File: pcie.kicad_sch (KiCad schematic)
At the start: 28 parts, among them J10 1-2199119-6, U1 MIMX8MM6DVTLZAA, U33 SI52112-B5-GM2, U34 74LVC2G07, Y4 25MHz

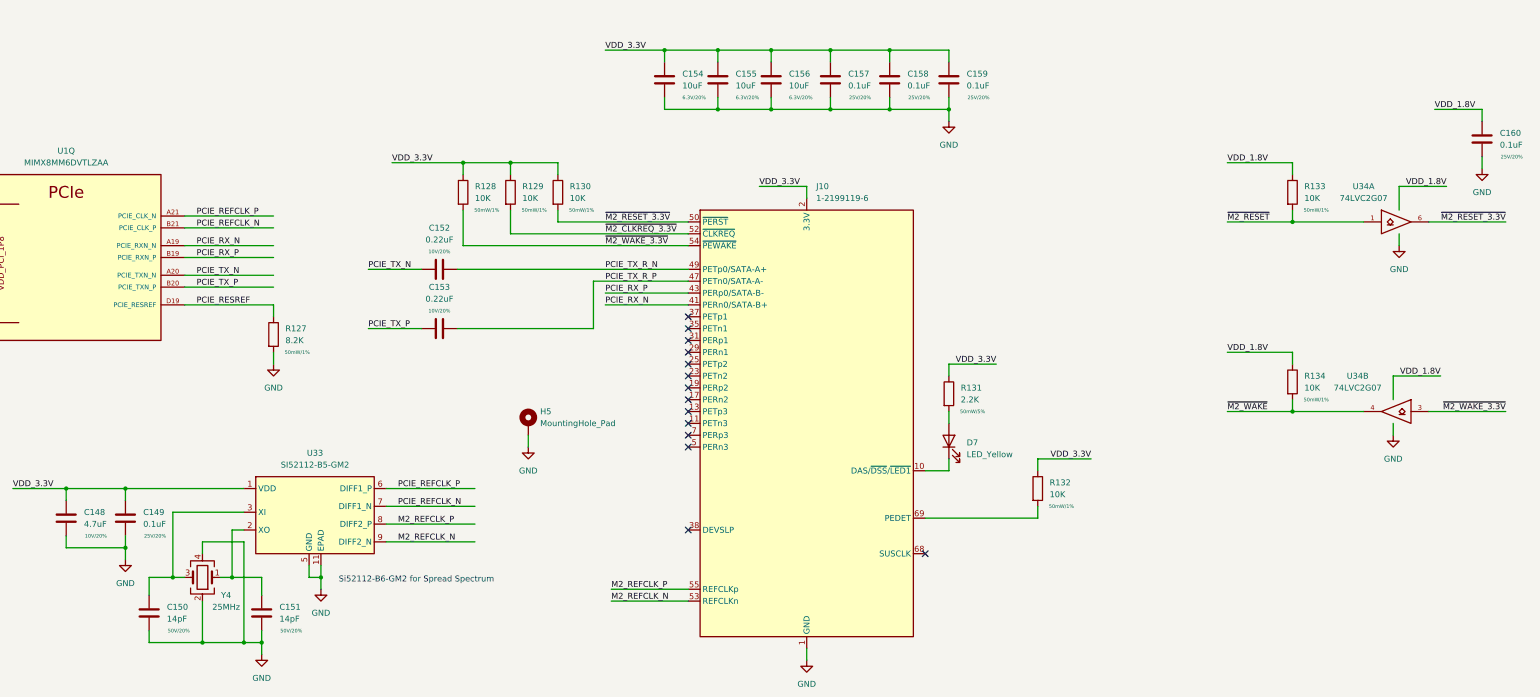
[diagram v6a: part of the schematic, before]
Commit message: ddr length matching work, misc cleanup
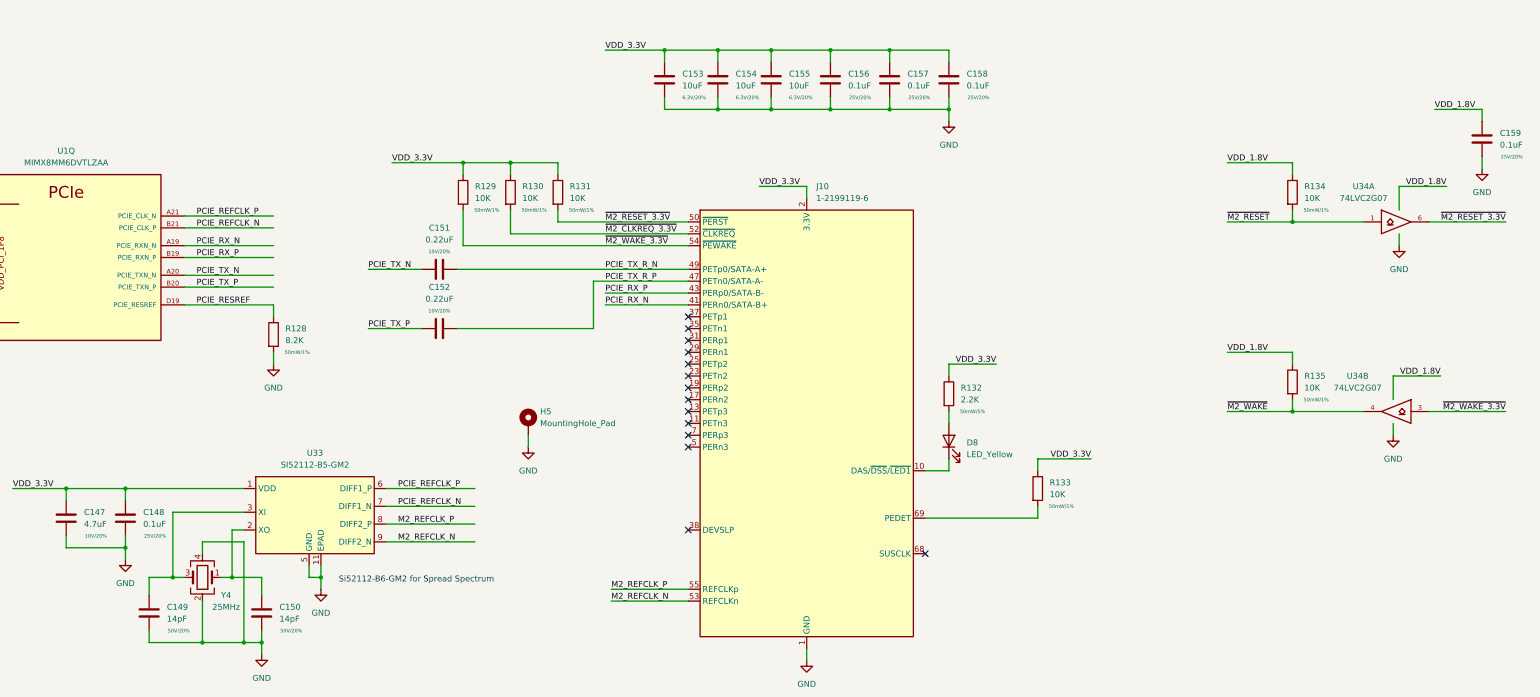
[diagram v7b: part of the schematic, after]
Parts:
- renumbered C148 to C147, C149 to C148, C150 to C149, C151 to C150, C152 to C151, C153 to C152, C154 to C153, C155 to C154, C156 to C155, C157 to C156, C158 to C157, C159 to C158, C160 to C159, D7 to D8, R127 to R128, R128 to R129, R129 to R130, R130 to R131, R131 to R132, R132 to R133, R133 to R134, R134 to R135
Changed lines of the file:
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@@
   (symbol (lib_id "power:GND") (at 236.22 154.94 0) (unit 1)
     (in_bom yes) (on_board yes) (fields_autoplaced)
-    (property "Reference" "#PWR0148" (id 0) (at 236.22 161.29 0)
+    (property "Reference" "#PWR0151" (id 0) (at 236.22 161.29 0)
       (effects (font (size 1.27 1.27)) hide)
     )
@@
   (symbol (lib_id "Device:C") (at 381 43.18 0) (unit 1)
     (in_bom yes) (on_board yes)
-    (property "Reference" "C160" (id 0) (at 384.81 41.9099 0)
+    (property "Reference" "C159" (id 0) (at 384.81 41.9099 0)
       (effects (font (size 1.27 1.27)) (justify left))
     )
@@
   (symbol (lib_id "Device:C") (at 254 30.48 0) (unit 1)
     (in_bom yes) (on_board yes)
-    (property "Reference" "C158" (id 0) (at 257.81 29.2099 0)
+    (property "Reference" "C157" (id 0) (at 257.81 29.2099 0)
       (effects (font (size 1.27 1.27)) (justify left))
     )
@@
   (symbol (lib_id "Device:R") (at 266.7 97.79 0) (unit 1)
     (in_bom yes) (on_board yes)
-    (property "Reference" "R131" (id 0) (at 269.24 96.5199 0)
+    (property "Reference" "R132" (id 0) (at 269.24 96.5199 0)
       (effects (font (size 1.27 1.27)) (justify left))
     )
@@
   (symbol (lib_id "power:GND") (at 119.38 153.67 0) (unit 1)
     (in_bom yes) (on_board yes) (fields_autoplaced)
-    (property "Reference" "#PWR0144" (id 0) (at 119.38 160.02 0)
+    (property "Reference" "#PWR0147" (id 0) (at 119.38 160.02 0)
       (effects (font (size 1.27 1.27)) hide)
     )
@@
   (symbol (lib_id "power:GND") (at 266.7 39.37 0) (unit 1)
     (in_bom yes) (on_board yes) (fields_autoplaced)
-    (property "Reference" "#PWR0149" (id 0) (at 266.7 45.72 0)
+    (property "Reference" "#PWR0152" (id 0) (at 266.7 45.72 0)
       (effects (font (size 1.27 1.27)) hide)
     )
@@
   (symbol (lib_id "Device:C") (at 266.7 30.48 0) (unit 1)
     (in_bom yes) (on_board yes)
-    (property "Reference" "C159" (id 0) (at 270.51 29.2099 0)
+    (property "Reference" "C158" (id 0) (at 270.51 29.2099 0)
       (effects (font (size 1.27 1.27)) (justify left))
     )
@@
   (symbol (lib_id "Device:C") (at 228.6 30.48 0) (unit 1)
     (in_bom yes) (on_board yes)
-    (property "Reference" "C156" (id 0) (at 232.41 29.2099 0)
+    (property "Reference" "C155" (id 0) (at 232.41 29.2099 0)
       (effects (font (size 1.27 1.27)) (justify left))
     )
@@
   (symbol (lib_id "power:GND") (at 121.92 91.44 0) (unit 1)
     (in_bom yes) (on_board yes) (fields_autoplaced)
-    (property "Reference" "#PWR0145" (id 0) (at 121.92 97.79 0)
+    (property "Reference" "#PWR0148" (id 0) (at 121.92 97.79 0)
       (effects (font (size 1.27 1.27)) hide)
     )
@@
   (symbol (lib_id "Device:R") (at 121.92 85.09 0) (unit 1)
     (in_bom yes) (on_board yes)
-    (property "Reference" "R127" (id 0) (at 124.46 83.8199 0)
+    (property "Reference" "R128" (id 0) (at 124.46 83.8199 0)
       (effects (font (size 1.27 1.27)) (justify left))
     )
@@
   (symbol (lib_id "Device:C") (at 241.3 30.48 0) (unit 1)
     (in_bom yes) (on_board yes)
-    (property "Reference" "C157" (id 0) (at 245.11 29.2099 0)
+    (property "Reference" "C156" (id 0) (at 245.11 29.2099 0)
       (effects (font (size 1.27 1.27)) (justify left))
     )
@@
   (symbol (lib_id "Device:C") (at 90.17 124.46 0) (unit 1)
     (in_bom yes) (on_board yes)
-    (property "Reference" "C149" (id 0) (at 93.98 123.1899 0)
+    (property "Reference" "C148" (id 0) (at 93.98 123.1899 0)
       (effects (font (size 1.27 1.27)) (justify left))
     )
@@
   (symbol (lib_id "Device:R") (at 340.36 54.61 0) (unit 1)
     (in_bom yes) (on_board yes)
-    (property "Reference" "R133" (id 0) (at 342.9 53.3399 0)
+    (property "Reference" "R134" (id 0) (at 342.9 53.3399 0)
       (effects (font (size 1.27 1.27)) (justify left))
     )
@@
   (symbol (lib_id "Device:C") (at 95.25 144.78 0) (unit 1)
     (in_bom yes) (on_board yes)
-    (property "Reference" "C150" (id 0) (at 99.06 143.5099 0)
+    (property "Reference" "C149" (id 0) (at 99.06 143.5099 0)
       (effects (font (size 1.27 1.27)) (justify left))
     )
@@
   (symbol (lib_id "Device:R") (at 172.72 54.61 0) (unit 1)
     (in_bom yes) (on_board yes)
-    (property "Reference" "R129" (id 0) (at 175.26 53.3399 0)
+    (property "Reference" "R130" (id 0) (at 175.26 53.3399 0)
       (effects (font (size 1.27 1.27)) (justify left))
     )
@@
   (symbol (lib_id "Device:R") (at 285.75 118.11 0) (unit 1)
     (in_bom yes) (on_board yes)
-    (property "Reference" "R132" (id 0) (at 288.29 116.8399 0)
+    (property "Reference" "R133" (id 0) (at 288.29 116.8399 0)
       (effects (font (size 1.27 1.27)) (justify left))
     )
@@
   (symbol (lib_id "Device:C") (at 157.48 83.82 90) (unit 1)
     (in_bom yes) (on_board yes)
-    (property "Reference" "C153" (id 0) (at 157.48 74.93 90))
+    (property "Reference" "C152" (id 0) (at 157.48 74.93 90))
     (property "Value" "0.22uF" (id 1) (at 157.48 77.47 90))
     (property "Footprint" "qsbc:C_0201_0603Metric" (id 2) (at 161.29 82.8548 0)
@@
   (symbol (lib_id "Device:R") (at 182.88 54.61 0) (unit 1)
     (in_bom yes) (on_board yes)
-    (property "Reference" "R130" (id 0) (at 185.42 53.3399 0)
+    (property "Reference" "R131" (id 0) (at 185.42 53.3399 0)
       (effects (font (size 1.27 1.27)) (justify left))
     )
@@
   (symbol (lib_id "power:GND") (at 90.17 133.35 0) (unit 1)
     (in_bom yes) (on_board yes) (fields_autoplaced)
-    (property "Reference" "#PWR0143" (id 0) (at 90.17 139.7 0)
+    (property "Reference" "#PWR0146" (id 0) (at 90.17 139.7 0)
       (effects (font (size 1.27 1.27)) hide)
     )
@@
   (symbol (lib_id "power:GND") (at 361.95 106.68 0) (unit 1)
     (in_bom yes) (on_board yes) (fields_autoplaced)
-    (property "Reference" "#PWR0150" (id 0) (at 361.95 113.03 0)
+    (property "Reference" "#PWR0153" (id 0) (at 361.95 113.03 0)
       (effects (font (size 1.27 1.27)) hide)
     )
@@
   (symbol (lib_id "power:GND") (at 363.22 66.04 0) (unit 1)
     (in_bom yes) (on_board yes) (fields_autoplaced)
-    (property "Reference" "#PWR0151" (id 0) (at 363.22 72.39 0)
+    (property "Reference" "#PWR0154" (id 0) (at 363.22 72.39 0)
       (effects (font (size 1.27 1.27)) hide)
     )
@@
   (symbol (lib_id "Device:C") (at 119.38 144.78 0) (unit 1)
     (in_bom yes) (on_board yes)
-    (property "Reference" "C151" (id 0) (at 123.19 143.5099 0)
+    (property "Reference" "C150" (id 0) (at 123.19 143.5099 0)
       (effects (font (size 1.27 1.27)) (justify left))
     )
@@
   (symbol (lib_id "Device:C") (at 77.47 124.46 0) (unit 1)
     (in_bom yes) (on_board yes)
-    (property "Reference" "C148" (id 0) (at 81.28 123.1899 0)
+    (property "Reference" "C147" (id 0) (at 81.28 123.1899 0)
       (effects (font (size 1.27 1.27)) (justify left))
     )
@@
   (symbol (lib_id "power:GND") (at 381 49.53 0) (unit 1)
     (in_bom yes) (on_board yes) (fields_autoplaced)
-    (property "Reference" "#PWR0152" (id 0) (at 381 55.88 0)
+    (property "Reference" "#PWR0155" (id 0) (at 381 55.88 0)
       (effects (font (size 1.27 1.27)) hide)
     )
@@
   (symbol (lib_id "Device:R") (at 162.56 54.61 0) (unit 1)
     (in_bom yes) (on_board yes)
-    (property "Reference" "R128" (id 0) (at 165.1 53.3399 0)
+    (property "Reference" "R129" (id 0) (at 165.1 53.3399 0)
       (effects (font (size 1.27 1.27)) (justify left))
     )
@@
   (symbol (lib_id "Device:LED") (at 266.7 107.95 90) (unit 1)
     (in_bom yes) (on_board yes) (fields_autoplaced)
-    (property "Reference" "D7" (id 0) (at 270.51 108.2674 90)
+    (property "Reference" "D8" (id 0) (at 270.51 108.2674 90)
       (effects (font (size 1.27 1.27)) (justify right))
     )
@@
   (symbol (lib_id "power:GND") (at 132.08 139.7 0) (unit 1)
     (in_bom yes) (on_board yes) (fields_autoplaced)
-    (property "Reference" "#PWR0146" (id 0) (at 132.08 146.05 0)
+    (property "Reference" "#PWR0149" (id 0) (at 132.08 146.05 0)
       (effects (font (size 1.27 1.27)) hide)
     )
@@
   (symbol (lib_id "Device:C") (at 217.17 30.48 0) (unit 1)
     (in_bom yes) (on_board yes)
-    (property "Reference" "C155" (id 0) (at 220.98 29.2099 0)
+    (property "Reference" "C154" (id 0) (at 220.98 29.2099 0)
       (effects (font (size 1.27 1.27)) (justify left))
     )
@@
   (symbol (lib_id "Device:C") (at 205.74 30.48 0) (unit 1)
     (in_bom yes) (on_board yes)
-    (property "Reference" "C154" (id 0) (at 209.55 29.2099 0)
+    (property "Reference" "C153" (id 0) (at 209.55 29.2099 0)
       (effects (font (size 1.27 1.27)) (justify left))
     )
@@
   (symbol (lib_id "Device:C") (at 157.48 71.12 90) (unit 1)
     (in_bom yes) (on_board yes)
-    (property "Reference" "C152" (id 0) (at 157.48 62.23 90))
+    (property "Reference" "C151" (id 0) (at 157.48 62.23 90))
     (property "Value" "0.22uF" (id 1) (at 157.48 64.77 90))
     (property "Footprint" "qsbc:C_0201_0603Metric" (id 2) (at 161.29 70.1548 0)
@@
   (symbol (lib_id "power:GND") (at 176.53 109.22 0) (unit 1)
     (in_bom yes) (on_board yes) (fields_autoplaced)
-    (property "Reference" "#PWR0147" (id 0) (at 176.53 115.57 0)
+    (property "Reference" "#PWR0150" (id 0) (at 176.53 115.57 0)
       (effects (font (size 1.27 1.27)) hide)
     )
@@
   (symbol (lib_id "Device:R") (at 340.36 95.25 0) (unit 1)
     (in_bom yes) (on_board yes)
-    (property "Reference" "R134" (id 0) (at 342.9 93.9799 0)
-      (effects (font (size 1.27 1.27)) (justify left))
-    )
+    (property "Reference" "R135" (id 0) (at 342.9 93.9799 0)
+      (effects (font (size 1.27 1.27)) (justify left))
+    )

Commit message: misc cleanup, change from usb mux to dual uart
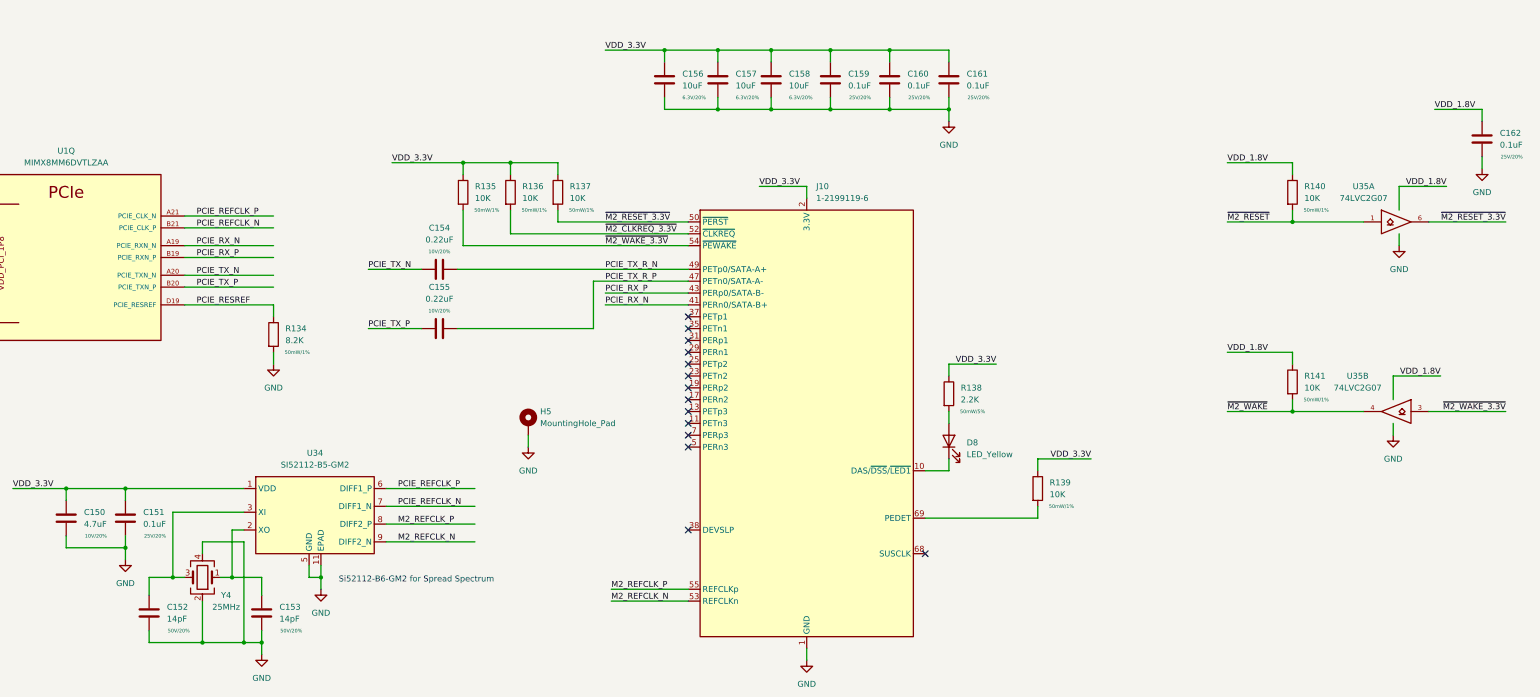
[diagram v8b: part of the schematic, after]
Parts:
- renumbered C147 to C150, C148 to C151, C149 to C152, C150 to C153, C151 to C154, C152 to C155, C153 to C156, C154 to C157, C155 to C158, C156 to C159, C157 to C160, C158 to C161, C159 to C162, R128 to R134, R129 to R135, R130 to R136, R131 to R137, R132 to R138, R133 to R139, R134 to R140, R135 to R141, U33 to U34, U34 to U35
